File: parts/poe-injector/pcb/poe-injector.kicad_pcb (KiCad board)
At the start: 2 copper layers, 58.4 x 30.9 mm, 17 parts, among them J1 Conn_01x01_Shielded, SW2 SW_SPDT

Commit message: clarify labels
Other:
- board text added: "DC+"
- board text added: "DC-"
- board text added: "PoE Inj + Surge Prot rev 1.5.1"
- board text removed: "+12V GND"
- board text removed: "PoE Inj + Surge Prot rev 1.5"
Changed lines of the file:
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@@
 			(at 8.890001 -0.2231 90)
 			(layer "F.SilkS")
+			(hide yes)
 			(effects
 				(font
@@
 			(at -7.1628 0.6096 0)
 			(layer "F.SilkS")
+			(hide yes)
 			(effects
 				(font
@@
 		(layer "Edge.Cuts")
 	)
-	(gr_text "(+)"
-		(at 118.872 22.2758 0)
-		(layer "F.SilkS")
-		(effects
-			(font
-				(size 1 1)
-				(thickness 0.15)
-			)
-			(justify left bottom)
-		)
-	)
-	(gr_text "+12V GND"
-		(at 82.0928 21.1328 180)
-		(layer "F.SilkS")
-		(effects
-			(font
-				(size 1.5 1.5)
-				(thickness 0.1875)
-			)
-		)
-	)
-	(gr_text "PoE Inj + Surge Prot rev 1.5"
-		(at 88.138 50.1904 0)
+	(gr_text "PoE Inj + Surge Prot rev 1.5.1"
+		(at 85.725 50.165 0)
 		(layer "F.SilkS")
 		(effects
@@
 		)
 	)
+	(gr_text "DC-"
+		(at 74.93 23.495 90)
+		(layer "F.SilkS")
+		(effects
+			(font
+				(size 2 2)
+				(bold yes)
+			)
+		)
+	)
+	(gr_text "DC+"
+		(at 89.535 21.59 180)
+		(layer "F.SilkS")
+		(effects
+			(font
+				(size 2 2)
+				(bold yes)
+			)
+		)
+	)
 	(gr_text "IN"
 		(at 80.4926 50.0126 0)
@@
 			(font
 				(size 3 3)
+			)
+			(justify left bottom)
+		)
+	)
+	(gr_text "(+)"
+		(at 118.11 21.59 0)
+		(layer "B.SilkS")
+		(effects
+			(font
+				(size 1 1)
+				(thickness 0.15)
 			)
 			(justify left bottom)
@@
 	)
 	(segment
-		(start 97.4511 22.7548)
+		(start 97.9555 22.2504)
 		(end 91.44 28.7659)
 		(width 0.4)
@@
 	)
 	(segment
-		(start 98.6028 22.2504)
-		(end 97.4511 22.2504)
+		(start 105.41 27.8279)
+		(end 105.41 22.242)
 		(width 0.4)
 		(layer "B.Cu")
@@
 	)
 	(segment
-		(start 105.41 27.8279)
-		(end 105.41 22.242)
+		(start 98.6028 22.2504)
+		(end 97.9555 22.2504)
 		(width 0.4)
 		(layer "B.Cu")
-		(net "Net-(SW2-A)")
-	)
-	(segment
-		(start 97.4511 22.2504)
-		(end 97.4511 22.7548)
-		(width 0.4)
-		(layer "B.Cu")

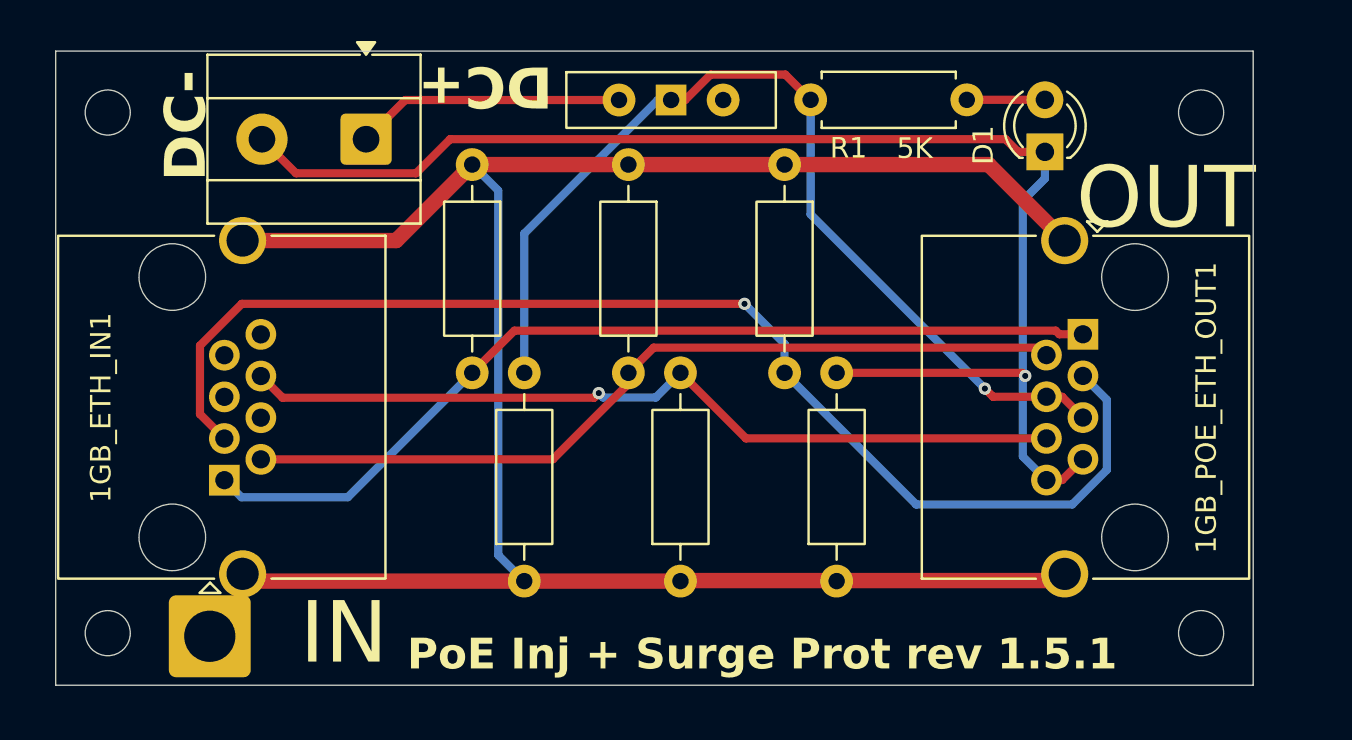
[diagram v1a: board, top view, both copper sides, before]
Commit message: round up dimensions of pcb
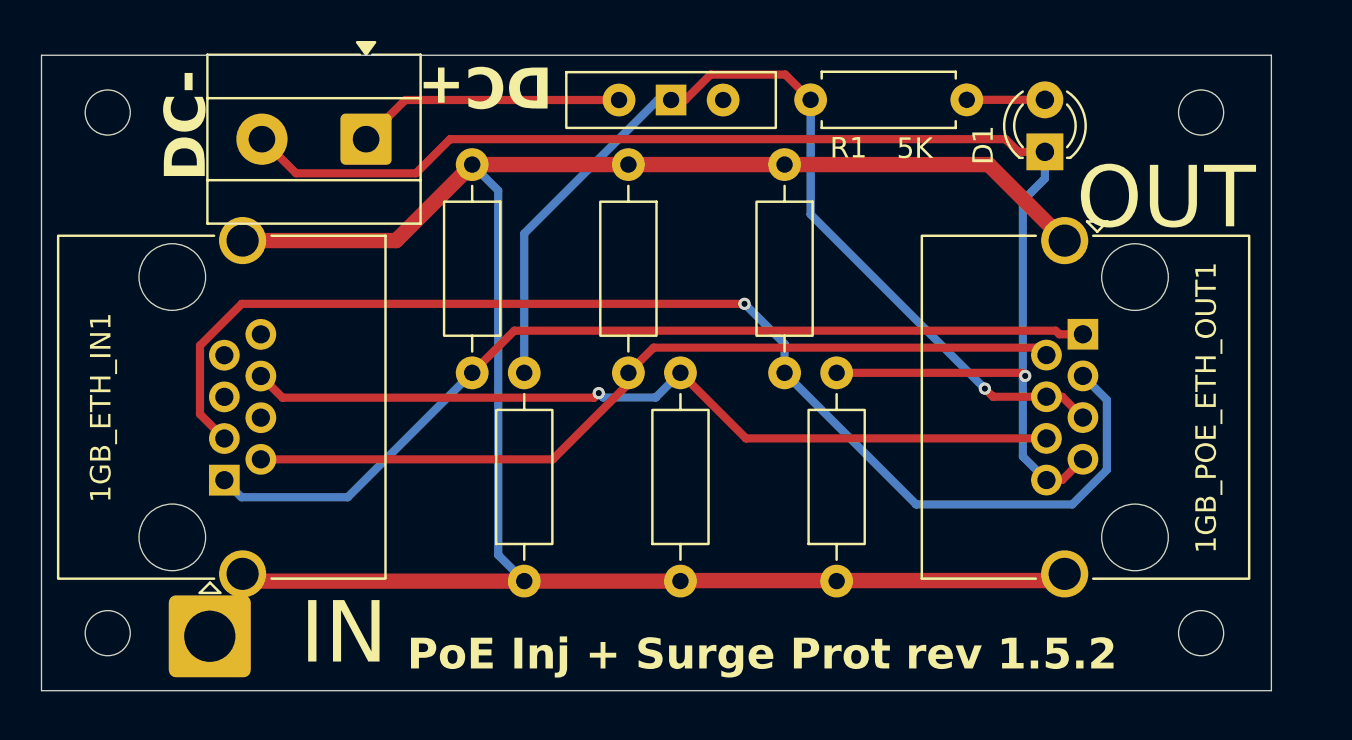
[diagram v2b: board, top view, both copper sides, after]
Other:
- board size 58.4 x 30.9 mm -> 60 x 31 mm
- board text added: "PoE Inj + Surge Prot rev 1.5.2"
- board text removed: "PoE Inj + Surge Prot rev 1.5.1"
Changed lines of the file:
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@@
 	)
 	(gr_rect
-		(start 68.58 19.8628)
-		(end 127 50.8)
+		(start 67.889 20.066)
+		(end 127.889 51.066)
 		(stroke
 			(width 0.05)
-			(type default)
+			(type solid)
 		)
 		(fill no)
 		(layer "Edge.Cuts")
 	)
-	(gr_text "PoE Inj + Surge Prot rev 1.5.1"
+	(gr_text "PoE Inj + Surge Prot rev 1.5.2"
 		(at 85.725 50.165 0)
 		(layer "F.SilkS")
